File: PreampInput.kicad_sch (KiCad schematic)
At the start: 20 parts, among them J202 XLR3, SW201 SW_DPDT_x2

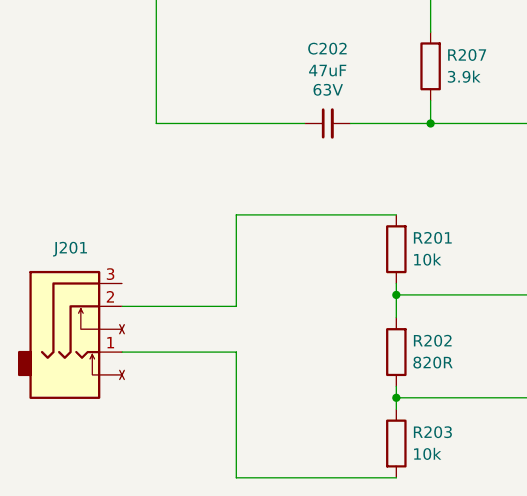
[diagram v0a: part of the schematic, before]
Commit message: Completed routing, cleanup, and artwork export
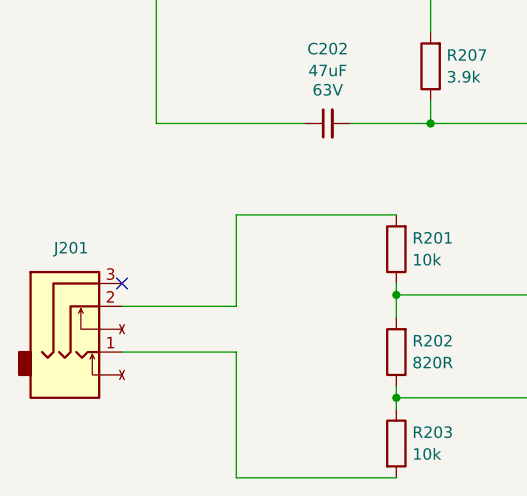
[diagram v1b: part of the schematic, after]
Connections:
- no-connect marks 0 -> 1
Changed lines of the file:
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@@
 		(color 0 0 0 0)
+	)
+	(no_connect
+		(at 46.99 105.41)
 	)
 	(wire

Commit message: Added schematic, assembly drawings, and assembly BoM exports
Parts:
- C201, C202: Source (none) -> MOUSER: 232-63PK47MEFC6.3X11
- C203, C204: Source (none) -> MOUSER: 232-25PX100MEFC5X11
- C205, C206, C207: Source (none) -> MOUSER: 810-FG18C0G1H101JNT0
- J201, J202: Source (none) -> MOUSER: 306-B3BXHALFSNP
- R201, R203: Source (none) -> MOUSER: 603-MFR-25FTF52-10K
- R202: Source (none) -> MOUSER: 603-MFR-25FBF52-820R
- R204, R207: Source (none) -> MOUSER: 603-MFR-25FBF52-3K9
- R205, R206: Source (none) -> MOUSER: 603-MFR-25FBF52-560R
- R208: Source (none) -> MOUSER: 603-MFR-25FRF52-3K3
- R209, R210: Source (none) -> MOUSER: 603-MFR-25FBF52-47K
- SW201: Source (none) -> MOUSER: 306-B6BXHALFSN
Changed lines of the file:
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@@
+			)
+		)
+		(property "Source" "MOUSER: 603-MFR-25FBF52-47K"
+			(at 151.13 97.79 0)
+			(effects
+				(font
+					(size 1.27 1.27)
+				)
+				(hide yes)
 			)
 		)
@@
 			)
 		)
+		(property "Source" "MOUSER: 810-FG18C0G1H101JNT0 "
+			(at 129.54 97.79 0)
+			(effects
+				(font
+					(size 1.27 1.27)
+				)
+				(hide yes)
+			)
+		)
 		(pin "1"
 		)
@@
 			)
 		)
+		(property "Source" "MOUSER: 603-MFR-25FBF52-820R"
+			(at 77.47 113.03 0)
+			(effects
+				(font
+					(size 1.27 1.27)
+				)
+				(hide yes)
+			)
+		)
 		(pin "2"
 		)
@@
 			)
 		)
+		(property "Source" "MOUSER: 603-MFR-25FBF52-3K9"
+			(at 81.28 43.18 0)
+			(effects
+				(font
+					(size 1.27 1.27)
+				)
+				(hide yes)
+			)
+		)
 		(pin "2"
 		)
@@
 			)
 		)
+		(property "Source" "MOUSER: 810-FG18C0G1H101JNT0 "
+			(at 125.73 60.96 0)
+			(effects
+				(font
+					(size 1.27 1.27)
+				)
+				(hide yes)
+			)
+		)
 		(pin "1"
 		)
@@
 		)
 		(property "Sim.Type" ""
+			(at 69.85 87.63 0)
+			(effects
+				(font
+					(size 1.27 1.27)
+				)
+				(hide yes)
+			)
+		)
+		(property "Source" "MOUSER: 232-63PK47MEFC6.3X11"
 			(at 69.85 87.63 0)
 			(effects
@@
 			)
 		)
+		(property "Source" "MOUSER: 603-MFR-25FBF52-47K"
+			(at 160.02 97.79 0)
+			(effects
+				(font
+					(size 1.27 1.27)
+				)
+				(hide yes)
+			)
+		)
 		(pin "2"
 		)
@@
 			)
 		)
+		(property "Source" "MOUSER: 603-MFR-25FRF52-3K3"
+			(at 111.76 62.23 0)
+			(effects
+				(font
+					(size 1.27 1.27)
+				)
+				(hide yes)
+			)
+		)
 		(pin "2"
 		)
@@
 			)
 		)
+		(property "Source" "MOUSER: 306-B6BXHALFSN"
+			(at 102.87 36.83 0)
+			(effects
+				(font
+					(size 1.27 1.27)
+				)
+				(hide yes)
+			)
+		)
 		(pin "1"
 		)
@@
 		)
 		(property "Sim.Type" ""
+			(at 118.11 36.83 0)
+			(effects
+				(font
+					(size 1.27 1.27)
+				)
+				(hide yes)
+			)
+		)
+		(property "Source" "MOUSER: 232-25PX100MEFC5X11"
 			(at 118.11 36.83 0)
 			(effects
@@
 			)
 		)
+		(property "Source" "MOUSER: 603-MFR-25FBF52-3K9"
+			(at 81.28 81.28 0)
+			(effects
+				(font
+					(size 1.27 1.27)
+				)
+				(hide yes)
+			)
+		)
 		(pin "2"
 		)
@@
 		)
 		(property "Sim.Type" ""
+			(at 77.47 123.19 0)
+			(effects
+				(font
+					(size 1.27 1.27)
+				)
+				(hide yes)
+			)
+		)
+		(property "Source" "MOUSER: 603-MFR-25FTF52-10K"
 			(at 77.47 123.19 0)
 			(effects
@@
 			)
 		)
+		(property "Source" "MOUSER: 306-B6BXHALFSN"
+			(at 104.14 90.17 0)
+			(effects
+				(font
+					(size 1.27 1.27)
+				)
+				(hide yes)
+			)
+		)
 		(pin "1"
 		)
@@
 			)
 		)
+		(property "Source" "MOUSER: 603-MFR-25FTF52-10K"
+			(at 77.47 101.6 0)
+			(effects
+				(font
+					(size 1.27 1.27)
+				)
+				(hide yes)
+			)
+		)
 		(pin "2"
 		)
@@
 			)
 		)
+		(property "Source" "MOUSER: 306-B3BXHALFSNP"
+			(at 41.91 110.49 0)
+			(effects
+				(font
+					(size 1.27 1.27)
+				)
+				(hide yes)
+			)
+		)
 		(pin "2"
 		)
@@
 			)
 		)
+		(property "Source" "MOUSER: 810-FG18C0G1H101JNT0 "
+			(at 140.97 97.79 0)
+			(effects
+				(font
+					(size 1.27 1.27)
+				)
+				(hide yes)
+			)
+		)
 		(pin "1"
 		)
@@
 			)
 		)
+		(property "Source" "MOUSER: 232-63PK47MEFC6.3X11"
+			(at 69.85 34.29 0)
+			(effects
+				(font
+					(size 1.27 1.27)
+				)
+				(hide yes)
+			)
+		)
 		(pin "1"
 		)
@@
 		)
 		(property "Sim.Type" ""
+			(at 118.11 90.17 0)
+			(effects
+				(font
+					(size 1.27 1.27)
+				)
+				(hide yes)
+			)
+		)
+		(property "Source" "MOUSER: 232-25PX100MEFC5X11"
 			(at 118.11 90.17 0)
 			(effects
@@
 			)
 		)
+		(property "Source" "MOUSER: 603-MFR-25FBF52-560R"
+			(at 81.28 54.61 0)
+			(effects
+				(font
+					(size 1.27 1.27)
+				)
+				(hide yes)
+			)
+		)
 		(pin "2"
 		)
@@
 			)
 		)
+		(property "Source" "MOUSER: 603-MFR-25FBF52-560R"
+			(at 81.28 66.04 0)
+			(effects
+				(font
+					(size 1.27 1.27)
+				)
+				(hide yes)
+			)
+		)
 		(pin "2"
 		)
@@
 			(at 50.8 57.15 0)
 			(effects
+				(font
+					(size 1.27 1.27)
+				)
+				(hide yes)
+			)
+		)
+		(property "Source" "MOUSER: 306-B3BXHALFSNP"
+			(at 50.8 57.15 0)
+			(effects
